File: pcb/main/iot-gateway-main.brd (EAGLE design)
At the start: 150 x 100 mm, 246 parts, among them CON1 6P-SH-TOP, CON2 2P-PH-TOP, CON3 6P-SH-TOP, CON4 3P-SH-TOP, CON5 5P-SH-TOP, CON6 2P-PH-TOP, Q1 AO3400, Q2 AO3400, Q3 AO3400, T1 BC817, U1 SST26VF064B, U10 BMP280, U11 CCS811, U12 ER-TFT035-6-BOT, U13 74LVC1G08, U14 74LVC1G08, U15 74LVC1G17, U16 LTC4313-1, U17 LT8636, U18 MIC23159, U19 74LVC1G04, U2 EFM32GG11B820F2048GQ100, U20 LTC2942, U21 LTC4040, U22 FS312F-G, U23 FS8205, U3 SST26VF016B, U4 ESP8266EX, U5 RFM69HW, U6 74LVC1G08, U7 SIM800C, U8 SI7021, U9 SI7210, X1 24 MHz, X2 32.768 kHz, X3 26 MHz

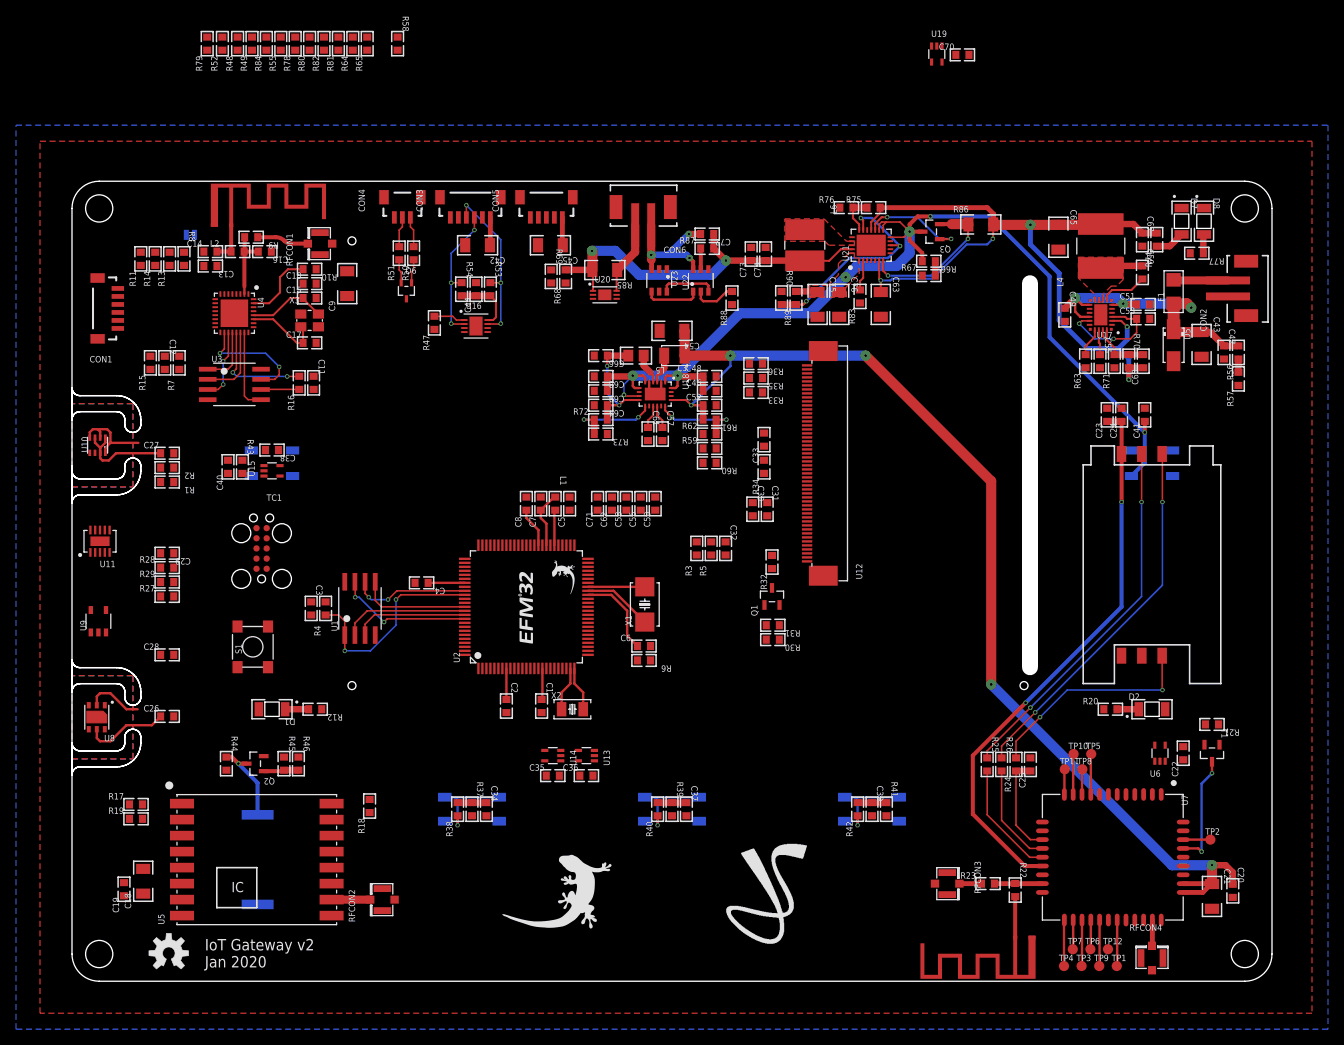
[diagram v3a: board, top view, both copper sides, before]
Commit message: Update libraries Finish routing Generate schematic PDF files
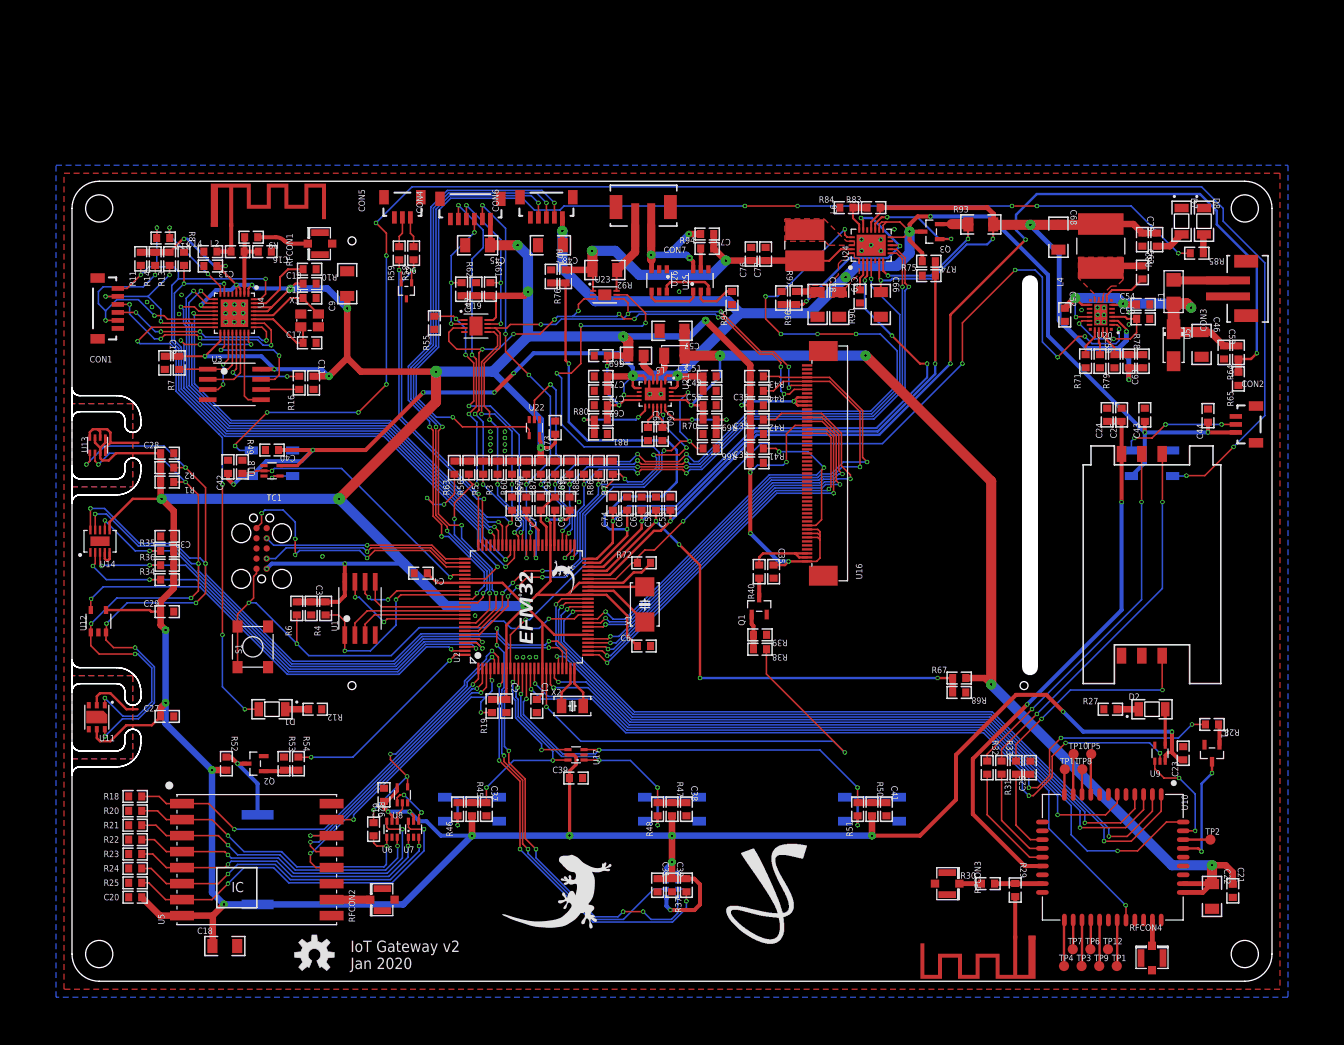
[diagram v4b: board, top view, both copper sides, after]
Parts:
- removed SJ1: (no value), Solder Jumper:SJ_S
- added C77: 10uF, Capacitor:CAP0603
- added C78: 100uF, Capacitor:CAP1206
- added C79: 22uF, Capacitor:CAP1206
- added CON7: 2P-PH-TOP, JST:PH-02-TOP
- added R91: 100K Ohms, Resistor:RES0603
- added R92: 25m Ohms, Resistor:RES1206
- added R93: 10m Ohms, Resistor:RES1206
- added R94, R95: 100 Ohms, Resistor:RES0603
- added R96: 1.5M Ohms, Resistor:RES0603
- added R97: 274K Ohms, Resistor:RES0603
- added U24: LTC4040, Analog Devices:QFN24_ASYM
- added U25: FS312F-G, Fortune:SOT23-6
- added U26: FS8205, Fortune:SOT23-6
- C21, C75: value 100uF -> 100nF; device Capacitor:CAP1206 -> Capacitor:CAP0603
- C22, C66: value 100nF -> 100uF; device Capacitor:CAP0603 -> Capacitor:CAP1206
- C23: value 33pF -> 100nF
- C24: value 1uF -> 33pF
- C25: value 33pF -> 1uF
- C26: value 100nF -> 33pF
- C30: value 10uF -> 100nF
- C31, C52: value 100nF -> 1uF
- C33, C67: value 100nF -> 10uF
- C34, C39: value 1nF -> 100nF
- C38, C41: value 100nF -> 1nF
- C42, C76: value 22uF -> 100nF; device Capacitor:CAP1206 -> Capacitor:CAP0603
- C43: value 10uF -> 100nF; device Capacitor:CAP1206 -> Capacitor:CAP0603
- C46: value 100nF -> 10uF; device Capacitor:CAP0603 -> Capacitor:CAP1206
- C47, C69: value 4.7uF -> 100nF
- C48: value 4.7uF -> 22uF; device Capacitor:CAP0603 -> Capacitor:CAP1206
- C49: value 1uF -> 100nF
- C50: value 470pF -> 4.7uF
- C51: value 1uF -> 4.7uF
- C53: value 1uF -> 470pF
- C54: value 100uF -> 1uF; device Capacitor:CAP1206 -> Capacitor:CAP0603
- C55: value 10nF -> 100nF
- C56: value 470pF -> 1uF
- C57: value 470pF -> 100uF; device Capacitor:CAP0603 -> Capacitor:CAP1206
- C58: value 470pF -> 10nF
- C59: value 100nF -> 470pF
- C60: value 10pF -> 470pF
- C62, C71: value 470pF -> 100nF
- C63: value 100uF -> 10pF; device Capacitor:CAP1206 -> Capacitor:CAP0603
- C64, C74: value 10uF -> 470pF
- C65: value 22uF -> 470pF; device Capacitor:CAP1206 -> Capacitor:CAP0603
- C68: value 100nF -> 22uF; device Capacitor:CAP0603 -> Capacitor:CAP1206
- C72: value 100nF -> 4.7uF
- CON2: value 2P-PH-TOP -> 3P-SH-TOP; device JST:PH-02-TOP -> JST:SH-03-TOP
- CON3: value 6P-SH-TOP -> 2P-PH-TOP; device JST:SH-06-TOP -> JST:PH-02-TOP
- CON4: value 3P-SH-TOP -> 6P-SH-TOP; device JST:SH-03-TOP -> JST:SH-06-TOP
- CON5: value 5P-SH-TOP -> 3P-SH-TOP; device JST:SH-05-TOP -> JST:SH-03-TOP
- CON6: value 2P-PH-TOP -> 5P-SH-TOP; device JST:PH-02-TOP -> JST:SH-05-TOP
- R1, R2, R3, R5: value 4.7K Ohms -> 2.2K Ohms
- R17: value 10K Ohms -> 0 Ohms
- R18, R34, R35: value 100K Ohms -> 10K Ohms
- R20, R77: value 330 Ohms -> 100K Ohms
- R21: value 10K Ohms -> 100K Ohms
- R22, R23: value 0 Ohms -> 100K Ohms
- R24, R25: value 22 Ohms -> 100K Ohms
- R26, R30: value 22 Ohms -> 0 Ohms
- R27: value 10K Ohms -> 330 Ohms
- R29: value 100K Ohms -> 0 Ohms
- R31: value 10K Ohms -> 22 Ohms
- R32: value 0 Ohms -> 22 Ohms
- R33: value 100K Ohms -> 22 Ohms
- R37, R41: value 1 MOhms -> 100K Ohms
- R38: value 100 Ohms -> 22 Ohms
- R39: value 1 MOhms -> 10K Ohms
- R40: value 100 Ohms -> 0 Ohms
- R42, R87, R88: value 100 Ohms -> 100K Ohms
- R44: value 1K Ohms -> 100K Ohms
- R45: value 10K Ohms -> 1 MOhms
- R46: value 22 Ohms -> 100 Ohms
- R47: value 100K Ohms -> 1 MOhms
- R48: value 100K Ohms -> 100 Ohms
- R50: value 33 Ohms -> 1 MOhms
- R51: value 33 Ohms -> 100 Ohms
- R52: value 100K Ohms -> 1K Ohms
- R53: value 4.7K Ohms -> 10K Ohms
- R54: value 4.7K Ohms -> 22 Ohms
- R56: value 147K Ohms -> 100K Ohms
- R57: value 21K Ohms -> 100K Ohms
- R58, R59: value 100K Ohms -> 33 Ohms
- R61: value 357K Ohms -> 4.7K Ohms
- R62: value 61.9K Ohms -> 4.7K Ohms
- R63: value 17.8K Ohms -> 100K Ohms
- R64: value 100K Ohms -> 147K Ohms
- R65: value 100K Ohms -> 21K Ohms
- R69: value 100K Ohms -> 357K Ohms
- R70: value 1M Ohms -> 61.9K Ohms
- R71: value 232K Ohms -> 17.8K Ohms
- R72: value 309K Ohms -> 100K Ohms
- R73: value 71.5K Ohms -> 100K Ohms
- R74: value 510 Ohms -> 100K Ohms
- R75: value 178K Ohms -> 100K Ohms
- R76: value 60.4K Ohms -> 100K Ohms
- R78: value 100K Ohms -> 1M Ohms
- R79: value 100K Ohms -> 232K Ohms
- R80: value 100K Ohms -> 309K Ohms
- R81: value 100K Ohms -> 71.5K Ohms
- R82: value 100K Ohms -> 510 Ohms
- R83: value 2K Ohms -> 178K Ohms
- R84: value 100K Ohms -> 57.6K Ohms
- R85: value 25m Ohms -> 330 Ohms; device Resistor:RES1206 -> Resistor:RES0603
- R86: value 10m Ohms -> 100K Ohms; device Resistor:RES1206 -> Resistor:RES0603
- R89: value 1.5M Ohms -> 100K Ohms
- R90: value 274K Ohms -> 2K Ohms
- U10: value BMP280 -> SIM800C; device Bosch:BMP280 -> SimCom:SIM800C
- U11: value CCS811 -> SI7021; device AMS:LGA10 -> Silicon Labs:DFN6
- U12: value ER-TFT035-6-BOT -> SI7210; device BuyDisplay:FPC-50P-TFT-BOT -> Silicon Labs:SOT23-5
- U13: value 74LVC1G08 -> BMP280; device Logic:SC70-5 -> Bosch:BMP280
- U14: value 74LVC1G08 -> CCS811; device Logic:SC70-5 -> AMS:LGA10
- U15: value 74LVC1G17 -> TMG39933; device Logic:SC70-5 -> AMS:LGA8
- U16: value LTC4313-1 -> ER-TFT035-6-BOT; device Analog Devices:DFN8 -> BuyDisplay:FPC-50P-TFT-BOT
- U17: value LT8636 -> 74LVC1G11; device Analog Devices:QFN20_ASYM_CORNER -> Logic:SC70-6
- U18: value MIC23159 -> 74LVC1G17; device Microchip:VQFN20 -> Logic:SC70-5
- U19: value 74LVC1G04 -> LTC4313-1; device Logic:SC70-5 -> Analog Devices:DFN8
- U20: value LTC2942 -> LT8636; device Analog Devices:DFN6 -> Analog Devices:QFN20_ASYM_CORNER
- U21: value LTC4040 -> MIC23159; device Analog Devices:QFN24_ASYM -> Microchip:VQFN20
- U22: value FS312F-G -> 74LVC1G04; device Fortune:SOT23-6 -> Logic:SC70-5
- U23: value FS8205 -> LTC2942; device Fortune:SOT23-6 -> Analog Devices:DFN6
- U6: value 74LVC1G08 -> 74LVC1G332; device Logic:SC70-5 -> Logic:SC70-6
- U7: value SIM800C -> 74LVC1G332; device SimCom:SIM800C -> Logic:SC70-6
- U8: value SI7021 -> 74LVC1G32; device Silicon Labs:DFN6 -> Logic:SC70-5
- U9: value SI7210 -> 74LVC1G08; device Silicon Labs:SOT23-5 -> Logic:SC70-5
- moved C20 137.2 mm to (7.90, 10.5), turned to 180 degrees
- moved U10 137.0 mm to (130.1, 15.5), turned to 270 degrees
- moved R21 135.2 mm to (7.90, 19.5), turned to 0 degrees
- moved U9 133.7 mm to (136.0, 28.5), turned to 0 degrees
- moved R28 132.1 mm to (142.5, 32.1), turned to 180 degrees
- moved R20 122.6 mm to (7.90, 21.3)
- moved R79 120.1 mm to (130.3, 77.5)
- moved R27 118.7 mm to (129.8, 34.0)
- moved R64 117.2 mm to (145.8, 78.6)
- moved R65 116.7 mm to (145.8, 75.3)
- moved R29 112.8 mm to (117.9, 11.4), turned to 270 degrees
- moved R78 111.5 mm to (132.1, 77.5), turned to 270 degrees
- moved R24 110.9 mm to (7.90, 14.1), turned to 0 degrees
- moved R22 110.2 mm to (7.90, 17.7), turned to 0 degrees
- moved R48 109.2 mm to (73.2, 21.5)
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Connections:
- net LED_DO renamed LED2_DI
- net US3_CLK_RFM renamed US3_CLK_ISM
- net US3_MISO_RFM renamed US3_MISO_ISM
- net US3_MOSI_RFM renamed US3_MOSI_ISM
- removed net !CCS811_IRQ: R29.1, U11.3, U2.97
- removed net !CCS811_RESET: R27.1, U11.2, U2.98
- removed net !CCS811_WAKE: R28.1, U11.7, U2.96
- removed net !GSM_RING: U2.19, U7.7
- removed net !US3_CS_RFM: R18.1, U2.4, U5.15
- removed net 5V0_PGOOD: R80.1, U2.7, U21.11
- removed net LED_DI_BUF: D3.4, U15.4
- removed net MAG_ALERT: U2.99, U9.5
- removed net N$1: U13.4, U14.2
- removed net RFM_IRQ: R19.2, U2.6, U5.2
- removed net RFM_RESET: R17.2, U2.5, U5.1
- removed net U0_CTS_GSM: U2.39, U7.4
- removed net U0_RTS_GSM: U2.40, U7.3
- removed net U0_RX_GSM: U2.38, U7.1
- removed net U0_TX_GSM: U2.37, U7.2
- removed net WIFI_IO16: SJ1.1, U4.8
- removed net WTIM2_CC2_TFT_BL: R30.1, U2.30
- new net !ALS_IRQ: R37.1, U15.7, U2.7
- new net !IAQ_IRQ: R36.1, U14.3, U2.97
- new net !IAQ_RESET: R34.1, U14.2, U2.98
- new net !IAQ_WAKE: R35.1, U14.7, U2.96
- new net !US3_CS_ISM: R19.1, U2.4, U5.15
- new net EXT_LED_DI: CON2.2, D4.2
- new net ISM_IRQ: R26.1, U2.6, U8.4
- new net ISM_IRQ0: R20.2, R26.2, U5.2, U6.1
- new net ISM_IRQ012: U6.4, U8.2
- new net ISM_IRQ1: R21.2, U5.3, U6.3
- new net ISM_IRQ2: R22.2, U5.4, U6.6
- new net ISM_IRQ3: R23.2, U5.5, U7.1
- new net ISM_IRQ345: U7.4, U8.1
- new net ISM_IRQ4: R24.2, U5.6, U7.3
- new net ISM_IRQ5: R25.2, U5.7, U7.6
- new net ISM_RESET: R18.2, U2.5, U5.1
- new net LED1_DI: D3.4, U18.4
- new net MAG_IRQ: U12.5, U2.99
- new net N$2: U15.5, U15.6
- new net TIM0_CC1_TFT_BL: R38.1, U2.18
- new net U1_CTS_GSM: U10.4, U2.39
- new net U1_RTS_GSM: U10.3, U2.40
- new net U1_RX_GSM: U10.1, U2.38
- new net U1_TX_GSM: U10.2, U2.37
- new net WIFI_RTC_WKUP: R17.1, U4.8
- net !5V0_BACKUP: now also R87.1, U22.2, U24.20; no longer R78.1, U19.2, U21.20
- net !BAT_CHRG: now also R89.1, U24.8; no longer R82.1, U21.8
- net !BAT_CHRG_EN: now also R91.1, U24.4; no longer R84.1, U21.4
- net !BAT_FAULT: now also R88.1, U24.9; no longer R81.1, U21.9
- net !FUEL_GAUGE_IRQ: now also R86.1, U23.5; no longer R79.1, U20.5
- net !GSM_DTR: now also U10.6; no longer U7.6
- net !GSM_PWRKEY: now also U10.39; no longer U7.39
- net !TFT_RESET: now also R41.1, U16.10; no longer R33.1, U12.10
- net !TFT_TOUCH_IRQ: now also R44.1, U16.46; no longer R36.1, U12.46
- net !TFT_TOUCH_RESET: now also R43.1, U16.47; no longer R35.1, U12.47
- net !UI_BTN1: now also C37.1, R45.1, R46.2, U17.6; no longer C34.1, R37.1, R38.2, U13.2
- net !UI_BTN2: now also C38.1, R47.1, R48.2, U17.1; no longer C37.1, R39.1, R40.2, U13.1
- net !UI_BTN3: now also C41.1, R50.1, R51.2, U17.3; no longer C39.1, R41.1, R42.2, U14.1
- net !UI_BTN_IRQ: now also U17.4; no longer U14.4
- net !US2_CS_TFT: now also R42.1, U16.38; no longer R34.1, U12.38
- net !USB_PD_IRQ: now also CON4.2, R57.1; no longer CON3.2, R49.1
- net !USB_VBUS_HV_EN: now also CON6.3; no longer CON5.3
- net !WIFI_RESET: now also R17.2; no longer SJ1.2
- net 3V3: now also C20.1, C23.1, C34.1, C39.1, C45.1, C47.1, C67.1, C69.1, C73.1, CON4.1, R19.2, R42.2, R43.2, R45.2, R47.2, R50.2, R56.2, R57.2, R60.2, R61.2, R62.2, R63.2, R73.2, R86.2, R87.2, R88.2, R89.2, R91.2, U11.5, U12.4, U13.2, U13.6, U13.8, U14.6, U15.1, U15.4, U16.1, U16.35, U16.40, U16.41, U16.42, U16.7, U16.9, U17.5, U19.8, U21.10, U22.5, U6.5, U7.5, U9.3; no longer C22.1, C26.1, C42.1, C44.1, C64.1, C66.1, C70.1, CON3.1, R18.2, R27.2, R28.2, R29.2, R33.2, R39.2, R48.2, R49.2, R53.2, R54.2, R55.2, R64.2, R65.2, R78.2, R79.2, R81.2, R82.2, R84.2, U10.2, U10.6, U10.8, U11.6, U12.1, U12.35, U12.40, U12.41, U12.42, U12.7, U12.8, U12.9, U13.5, U14.5, U18.10, U19.5, U6.3, U9.4
- net 3V3_FB: now also R80.1, R81.2, U21.11; no longer R72.1, R73.2, U18.11
- net 3V3_SS: now also C64.1, U21.13; no longer C61.1, U18.13
- net 3V3_SW: now also U21.4; no longer U18.4
- net 4V2: now also C22.1, C55.1, C57.1, R67.2, R69.2, U10.34, U10.35, U21.17; no longer C20.1, C52.1, C54.1, R59.2, R61.2, U18.17, U7.34, U7.35
- net 4V2_EN: now also R66.2, U21.18; no longer R58.2, U18.18
- net 4V2_FB: now also R69.1, R70.2, U21.16; no longer R61.1, R62.2, U18.16
- net 4V2_PGOOD: now also R73.1, U21.15; no longer R65.1, U18.15
- net 4V2_SS: now also C60.1, U21.14; no longer C57.1, U18.14
- net 4V2_SW: now also U21.3; no longer U18.3
- net 4V2_VSENSE: now also C59.1, R67.1, R68.2; no longer C56.1, R59.1, R60.2
- net 5V0: now also C42.1, C43.1, C44.1, C49.1, C51.1, C71.1, C72.1, C78.1, C79.1, CON2.1, CON6.1, R74.2, R96.2, U18.5, U21.20, U21.6, U21.7, U21.9, U24.1, U24.12, U24.13, U24.14, U24.24; no longer C38.1, C41.1, C45.1, C46.1, C68.1, C69.1, C75.1, C76.1, CON5.1, R66.2, R89.2, U15.5, U18.1, U18.20, U18.6, U18.7, U18.9, U21.12, U21.13, U21.14, U21.24
- net 5V0_BACKUP: now also R85.2, U22.4; no longer R77.2, U19.4
- net 5V0_FB: now also R96.1, R97.2, U24.10, U24.18; no longer R89.1, R90.2, U21.10, U21.18
- net 5V0_ISENSE: now also C74.1, U24.3; no longer C71.1, U21.3
- net 5V0_NBU: now also R93.1, U24.7; no longer R86.1, U21.7
- net 5V0_NBU_NSENS: now also C66.1, C68.1, C70.1, R78.2, R82.2, R83.2, R93.2, U20.2, U24.16, U24.6; no longer C60.1, C65.1, C67.1, R70.2, R74.2, R75.2, R86.2, U17.2, U21.16, U21.6
- net 5V0_NBU_NSENS_BST: now also C62.2, U20.7; no longer C59.2, U17.7
- net 5V0_NBU_NSENS_FB: now also C63.2, R78.1, R79.2, U20.19, U20.20; no longer C60.2, R70.1, R71.2, U17.19, U17.20
- net 5V0_NBU_NSENS_INTVCC: now also C56.1, U20.15, U20.3; no longer C53.1, U17.15, U17.3
- net 5V0_NBU_NSENS_PGOOD: now also R72.1, U20.1; no longer R64.1, U17.1
- net 5V0_NBU_NSENS_RT: now also R71.2, U20.17; no longer R63.2, U17.17
- net 5V0_NBU_NSENS_SS: now also C58.1, U20.18; no longer C55.1, U17.18
- net 5V0_NBU_NSENS_SW: now also C62.1, U20.10, U20.8, U20.9; no longer C59.1, U17.10, U17.8, U17.9
- net 5V0_VSENSE: now also C61.1, R74.1, R75.2; no longer C58.1, R66.1, R67.2
- net BAT_CHRG_PROG: now also R90.2, U24.2; no longer R83.2, U21.2
- net BAT_OC: now also U25.3, U26.6; no longer U22.3, U23.6
- net BAT_OD: now also U25.1, U26.4; no longer U22.1, U23.4
- net BAT_PROT_CS: now also R95.2, U25.2; no longer R88.2, U22.2
- net BAT_PROT_VCC: now also R94.1, U25.5; no longer R87.1, U22.5
- net BT_ANT: now also R29.1, R30.2, U10.20; no longer R22.1, R23.2, U7.20
- net BT_ANT_EXT: now also R30.1; no longer R23.1
- net BT_ANT_INT: now also R29.2; no longer R22.2
- net BUZZ_DRV: now also R52.1; no longer R44.1
- net CCS811_HEATER_PWM: now also U14.4, U14.5; no longer U11.4, U11.5
- net DCJACK_DET: now also CON4.5, R56.1; no longer CON3.5, R48.1
- net GBAT: now also C75.2, CON7.2, U25.6, U26.3; no longer C72.2, CON6.2, U22.6, U23.3
- net GND: now also C59.2, C60.2, C72.2, C77.2, C78.2, C79.2, CON2.3, CON3.2, CON4.6, CON5.3, CON6.5, R18.1, R21.1, R22.1, R23.1, R24.1, R25.1, R27.1, R39.1, R49.1, R53.1, R55.1, R65.1, R66.1, R68.1, R70.1, R75.1, R77.1, R79.1, R81.1, R84.1, R95.1, R97.1, U10.13, U10.19, U10.21, U10.27, U10.30, U10.31, U10.33, U10.36, U10.37, U10.8, U11.2, U12.2, U13.1, U13.5, U13.7, U14.1, U14.11, U16.11, U16.12, U16.13, U16.14, U16.15, U16.16, U16.17, U16.18, U16.19, U16.20, U16.21, U16.22, U16.23, U16.24, U16.25, U16.26, U16.27, U16.28, U16.29, U16.30, U16.31, U16.32, U16.43, U16.48, U16.49, U16.50, U17.2, U18.3, U19.4, U19.9, U20.12, U20.13, U20.21, U20.4, U20.5, U20.M1, U20.M2, U20.M3, U20.M4, U21.19, U21.2, U21.21, U21.8, U22.3, U23.2, U24.17, U24.25, U24.5, U26.1, U6.2, U7.2, U8.3, U9.5; no longer C62.2, C63.2, C75.2, CON2.2, CON3.6, CON4.3, CON5.5, R17.1, R19.1, R31.1, R43.1, R45.1, R47.1, R57.1, R58.1, R60.1, R62.1, R63.1, R67.1, R69.1, R73.1, R76.1, R83.1, R88.1, U10.1, U10.5, U10.7, U11.1, U11.PAD, U12.11, U12.12, U12.13, U12.14, U12.15, U12.16, U12.17, U12.18, U12.19, U12.20, U12.21, U12.22, U12.23, U12.24, U12.25, U12.26, U12.27, U12.28, U12.29, U12.30, U12.31, U12.32, U12.43, U12.48, U12.49, U12.50, U13.3, U14.3, U16.4, U16.9, U17.12, U17.13, U17.21, U17.4, U17.5, U17.M1, U17.M2, U17.M3, U17.M4, U18.19, U18.2, U18.21, U18.5, U18.8, U19.3, U20.2, U21.17, U21.25, U23.1, U6.5, U7.13, U7.19, U7.21, U7.27, U7.30, U7.31, U7.33, U7.36, U7.37, U7.8, U8.2, U9.2
- net GSM_2V8: now also U10.40; no longer U7.40
- net GSM_ANT: now also U10.32; no longer U7.32
- net GSM_LED: now also U9.4; no longer U6.4
- net GSM_LED_EN: now also U9.2; no longer U6.2
- net GSM_MIC+: now also U10.9; no longer U7.9
- net GSM_MIC-: now also U10.10; no longer U7.10
- net GSM_NETLIGHT: now also U10.41, U9.1; no longer U6.1, U7.41
- net GSM_PWRKEY: now also R28.2; no longer R21.2
- net GSM_RF_SYNC: now also U10.29, U2.19; no longer U2.18, U7.29
- net GSM_SPK+: now also U10.11; no longer U7.11
- net GSM_SPK-: now also U10.12; no longer U7.12
- net GSM_STATUS: now also U10.42; no longer U7.42
- net GSM_UART2_RX: now also U10.23; no longer U7.23
- net GSM_UART2_TX: now also U10.22; no longer U7.22
- net GSM_USB_D+: now also U10.25; no longer U7.25
- net GSM_USB_D-: now also U10.26; no longer U7.26
- net GSM_USB_VBUS: now also U10.24; no longer U7.24
- net GSM_VRTC: now also U10.28; no longer U7.28
- net I2C0_SCL_SYS: now also U16.44, U19.3, U23.3; no longer U12.44, U16.3, U20.3
- net I2C0_SDA_SYS: now also U16.45, U19.6, U23.4; no longer U12.45, U16.6, U20.4
- net I2C1_SCL_SENS: now also U11.6, U12.3, U13.4, U14.10, U15.2; no longer U10.4, U11.10, U8.6, U9.3
- net I2C1_SDA_SENS: now also U11.1, U12.1, U13.3, U14.9, U15.8; no longer U10.3, U11.9, U8.1, U9.1
- net I2C_SCL_USB_PD: now also CON4.3, R62.1, U19.2; no longer CON3.3, R54.1, U16.2
- net I2C_SDA_USB_PD: now also CON4.4, R61.1, U19.7; no longer CON3.4, R53.1, U16.7
- net N$16: now also R27.2; no longer R20.2
- net N$24: now also R38.2, R39.2; no longer R30.2, R31.2
- net N$28: now also R28.1; no longer R21.1
- net N$34: now also R53.2, R54.2; no longer R45.2, R46.2
- net N$37: now also U24.15; no longer U21.15
- net N$53: now also R46.1; no longer R38.1
- net N$57: now also R51.1; no longer R42.1
- net N$59: now also R48.1; no longer R40.1
- net N$63: now also CON5.2, R59.2; no longer CON4.2, R51.2
- net N$64: now also CON5.1, R58.2; no longer CON4.1, R50.2
- net N$91: now also R82.1; no longer R74.1
- net N$92: now also R85.1; no longer R77.1
- net PF_THRESH: now also R83.1, R84.2, U24.19; no longer R75.1, R76.2, U21.19
- net SIM_CLK: now also R33.2, U10.16; no longer R26.2, U7.16
- net SIM_CLK_FILT: now also R33.1; no longer R26.1
- net SIM_DATA: now also C26.1, R31.1, U10.15; no longer C25.1, R24.1, U7.15
- net SIM_DATA_FILT: now also R31.2; no longer R24.2
- net SIM_RST: now also R32.2, U10.17; no longer R25.2, U7.17
- net SIM_RST_FILT: now also R32.1; no longer R25.1
- net SIM_VDD: now also C25.1, U10.18; no longer C23.1, U7.18
- net TFT_BACKLIGHT_DRIVER: now also R40.1; no longer R32.1
- net TFT_BACKLIGHT_PWM: now also R40.2, U16.2, U16.3; no longer R32.2, U12.2, U12.3
- net TFT_DC: now also U16.37, U2.30; no longer U12.37
- net TIM3_CC2_BUZZ: now also R54.1; no longer R46.1
- net TIM4_CC2_LED_DI: now also R49.2, U18.2; no longer R43.2, U15.2
- net US2_CLK_TFT: now also U16.36; no longer U12.36
- net US2_MISO_TFT: now also U16.33; no longer U12.33
- net US2_MOSI_TFT: now also U16.34; no longer U12.34
- net USB_D+: now also R58.1; no longer R50.1
- net USB_D-: now also R59.1; no longer R51.1
- net USB_PD_I2C_EN: now also R55.2, U19.1; no longer R47.2, U16.1
- net USB_PD_I2C_READY: now also R60.1, U19.5; no longer R52.1, U16.5
- net USB_VBUS_HV_STAT: now also CON6.2, R63.1; no longer CON5.2, R55.1
- net USB_VBUS_SUP_EN: now also CON6.4; no longer CON5.4
- net VBAT: now also C75.1, C76.1, C77.1, R76.2, R92.2, R94.2, U23.1, U24.23; no longer C72.1, C73.1, C74.1, R68.2, R85.2, R87.2, U20.1, U21.23
- net VBAT_NSENS: now also CON7.1, R92.1, U23.6; no longer CON6.1, R85.1, U20.6
- net VBAT_SW: now also U24.21, U24.22; no longer U21.21, U21.22
- net VBAT_VSENSE: now also C65.1, R76.1, R77.2; no longer C62.1, R68.1, R69.2
- net VIN: now also C46.1, C50.1, C52.1, C54.1, R64.2, U20.11, U20.14, U20.6; no longer C43.1, C47.1, C49.1, C51.1, R56.2, U17.11, U17.14, U17.6
- net VIN_UNFUSED: now also CON3.1; no longer CON2.1
- net VIN_VSENSE: now also C53.1, R64.1, R65.2; no longer C50.1, R56.1, R57.2
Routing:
- net 3V3: track 72.8 -> 814.1 mm, vias 2 -> 45
- net I2C1_SCL_SENS: track 0.00 -> 199.9 mm, vias 0 -> 13
- net LED2_DI: track 0.00 -> 196.8 mm, vias 0 -> 8
- net I2C1_SDA_SENS: track 0.00 -> 194.5 mm, vias 0 -> 13
- net 5V0_BACKUP: track 0.00 -> 138.9 mm, vias 0 -> 6
- net VIN_VSENSE: track 1.66 -> 131.8 mm, vias 0 -> 4
- net !5V0_BACKUP: track 0.00 -> 117.8 mm, vias 0 -> 10
- net 5V0: track 142.4 -> 253.6 mm, vias 7 -> 14
- net !WIFI_RESET: track 0.00 -> 101.4 mm, vias 0 -> 4
- net 5V0_NBU_NSENS_PGOOD: track 0.00 -> 99.4 mm, vias 0 -> 6
- net GSM_PWRKEY: track 0.00 -> 97.3 mm, vias 0 -> 4
- net U1_RX_GSM: track 0.00 -> 97.1 mm, vias 0 -> 2
- net U1_RTS_GSM: track 0.00 -> 96.3 mm, vias 0 -> 2
- net GSM_LED_EN: track 0.00 -> 93.8 mm, vias 0 -> 4
- net U1_TX_GSM: track 0.00 -> 93.8 mm, vias 0 -> 2
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
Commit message: Start machine gun process
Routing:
- net GND: vias 48 -> 1620

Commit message: Maybe finished?
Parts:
- added TP13, TP14: TESTPOINT-1.27MM, PADs:PAD1.27MM
- R95: value 100 Ohms -> 2K Ohms
- moved C65 1.80 mm to (67.6, 59.7)
- moved C74 1.80 mm to (69.4, 59.7)
- moved CON4 0.20 mm to (49.8, 97.1)
- moved C44 0.10 mm to (142.0, 70.8)
- renumbered U26 to Q4
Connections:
- net TFT_DC renamed TFT_D/!C!
- removed net 5V0_ISENSE: C74.1, U2.50, U24.3
- new net !GSM_DCD: TP14.TP, U10.5
- new net !GSM_RING: TP13.TP, U10.7
- new net 5V0_NBU_ISENSE: C74.1, U2.49, U24.3
- net VBAT_VSENSE: now also U2.50; no longer U2.49
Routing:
- net 5V0_ISENSE: track 73.3 -> 0.00 mm, vias 4 -> 0
- net 5V0_NBU_ISENSE: track 0.00 -> 72.1 mm, vias 0 -> 4
- net VBAT_VSENSE: track 62.7 -> 56.3 mm
- net !GSM_DCD: track 0.00 -> 5.07 mm
- net !GSM_RING: track 0.00 -> 5.07 mm
- net WIFI_LED: track 65.9 -> 63.9 mm
- net GND: vias 1620 -> 1619
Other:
- board text added: "BT"
- board text added: "GSM"
- board text added: "ISM"
- board text added: "Wi-Fi"

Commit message: Fix ADC precision loss by right shift instead of dividing (already fixed before but came back?)
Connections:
- net N$37 renamed 5V0_GATE
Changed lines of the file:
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@@
 <wire x1="112.0108" y1="92.8108" x2="112.0108" y2="94.6398" width="0.254" layer="1"/>
 </signal>
-<signal name="N$37">
+<signal name="5V0_GATE">
 <contactref element="U24" pad="15"/>
 <contactref element="Q3" pad="1"/>

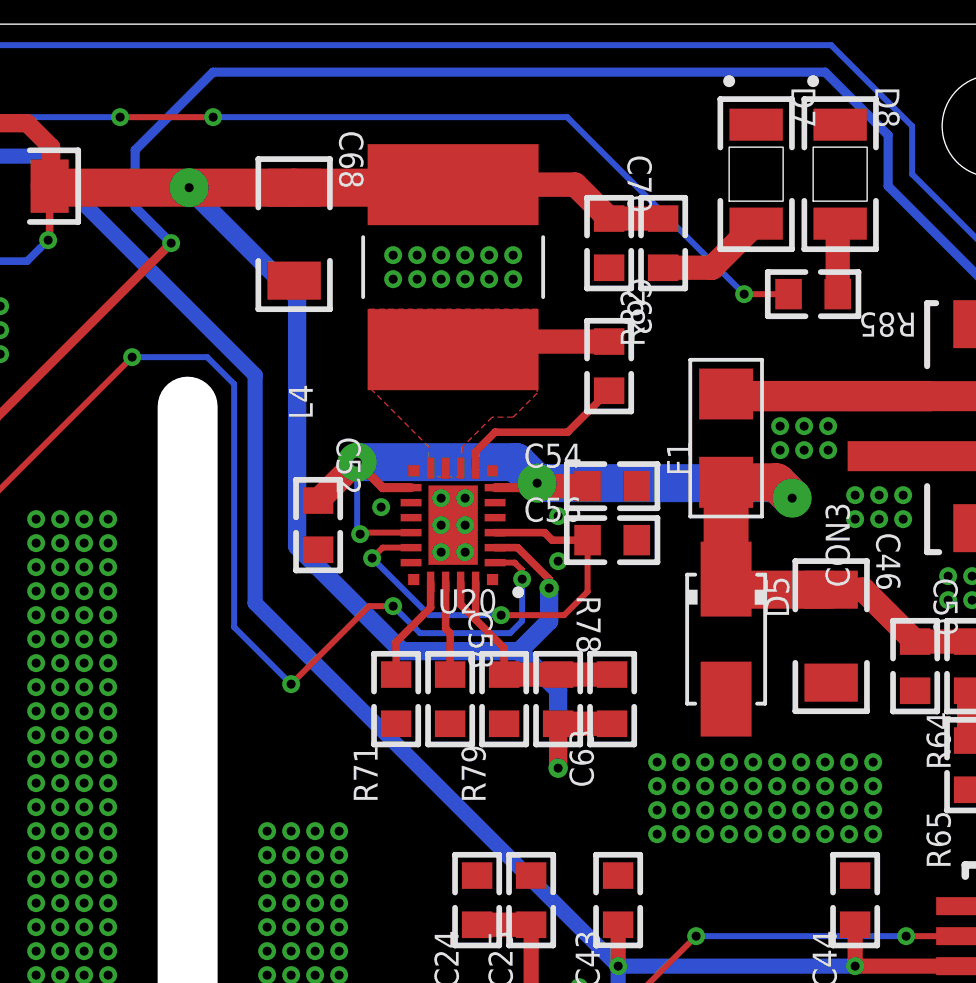
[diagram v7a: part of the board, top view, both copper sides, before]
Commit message: Change 5V_NBU regulator to LT8640S
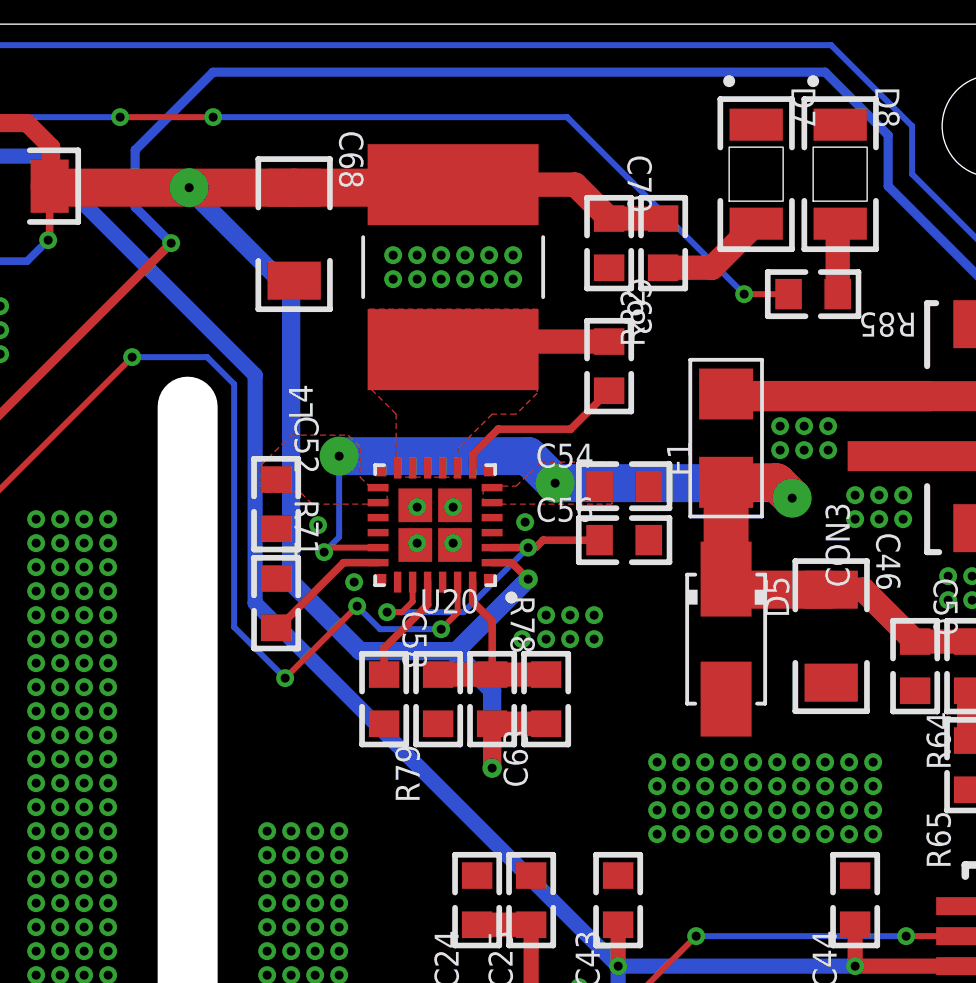
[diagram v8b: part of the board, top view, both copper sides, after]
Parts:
- R71: value 17.8K Ohms -> 41.2K Ohms
- U20: value LT8636 -> LT8640S; device Analog Devices:QFN20_ASYM_CORNER -> Analog Devices:QFN24_CORNER
- moved R71 5.12 mm to (122.7, 80.7), turned to 270 degrees
- moved C63 2.20 mm to (131.7, 77.5)
- moved R79 2.20 mm to (128.1, 77.5)
- moved C58 2.20 mm to (126.3, 77.5)
- moved R78 2.20 mm to (129.9, 77.5)
- moved C52 1.57 mm to (122.7, 84.0)
- moved U20 0.60 mm to (128.0, 83.3)
- moved C54 0.40 mm to (134.3, 84.6)
- moved C56 0.40 mm to (134.3, 82.8)
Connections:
- net 5V0_NBU_NSENS: now also U20.1; no longer U20.2
- net 5V0_NBU_NSENS_FB: now also U20.24; no longer U20.19, U20.20
- net 5V0_NBU_NSENS_INTVCC: now also U20.2, U20.20; no longer U20.15, U20.3
- net 5V0_NBU_NSENS_PGOOD: now also U20.23; no longer U20.1
- net 5V0_NBU_NSENS_RT: now also U20.18; no longer U20.17
- net 5V0_NBU_NSENS_SS: now also U20.21; no longer U20.18
- net 5V0_NBU_NSENS_SW: now also U20.11, U20.12
- net GND: now also U20.16, U20.22, U20.25, U20.26, U20.27, U20.28, U20.29, U20.3, U20.30, U20.31, U20.32; no longer U20.12, U20.13, U20.21, U20.4, U20.5, U20.M1, U20.M2, U20.M3, U20.M4
- net VIN: now also U20.13, U20.17, U20.5; no longer U20.11
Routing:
- net VIN: track 41.0 -> 35.6 mm
- net 5V0_NBU_NSENS_PGOOD: track 99.4 -> 95.4 mm
- net 5V0_NBU_NSENS_INTVCC: track 14.6 -> 10.9 mm
- net 5V0_NBU_NSENS_FB: track 8.53 -> 6.95 mm
- net 5V0_NBU_NSENS: track 97.1 -> 95.6 mm
- net 5V0_NBU_NSENS_RT: track 3.56 -> 4.30 mm
- net 5V0_NBU_NSENS_SS: track 3.14 -> 3.68 mm
- net GND: vias 1619 -> 1624
- added copper zone on layer 1, net VIN
